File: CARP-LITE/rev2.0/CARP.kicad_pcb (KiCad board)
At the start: 4 copper layers, 70.1 x 40 mm, 154 parts, among them J1 USB-C, J10 PYRO_2, J11 RF_L, J3 I2C1+3V3, J4 2S XT30, J5 UART+5V+I2C1, J6 PYRO_1, J7 RF_H, J8 PWM1+5V1, J9 PWM2+5V1, Q5 SQ2318CES, Q6 SQ2318CES, Q7 SQ2318CES, SW1 SW_Push, SW2 SW_Push, U1 W25Q128JVSIMTR (16MB), U10 TPS62130A, U2 W25Q32RVXHJQ (2MB), U4 RP2350_60QFN, U5 LSM6DSO, U6 BMP390, U7 TLV75733PDBV, U9 LR2021IMLTRT, Y1 ABM8-272-T3, Y2 ECS-TXO-25CSMV-320-AN-TR

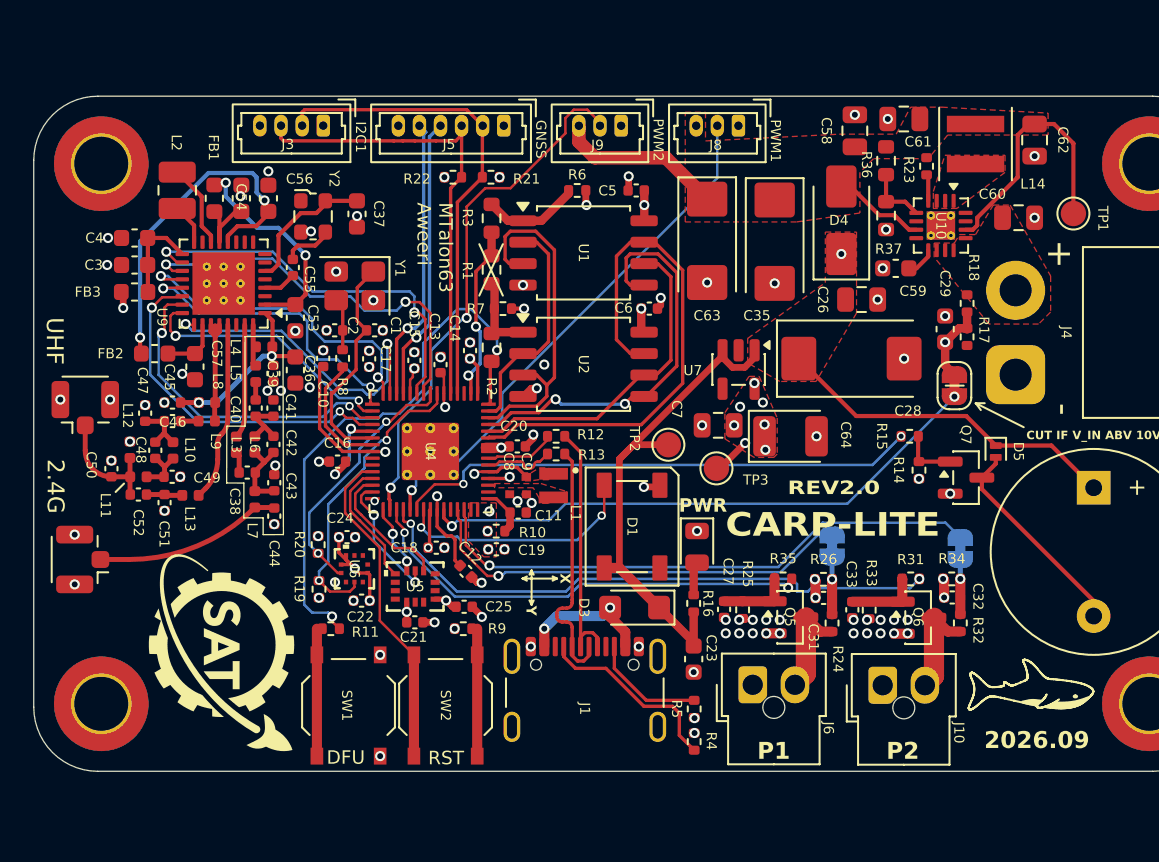
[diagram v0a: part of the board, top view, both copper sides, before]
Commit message: move vias from pads
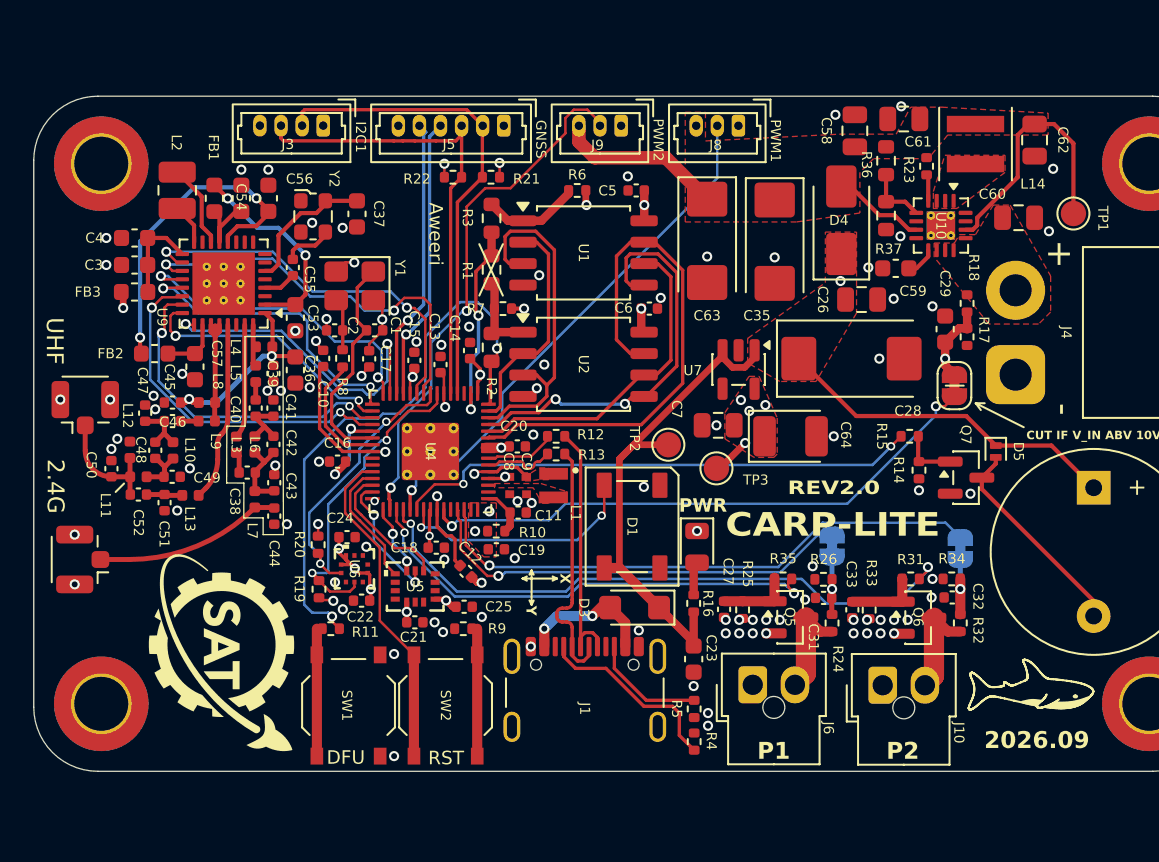
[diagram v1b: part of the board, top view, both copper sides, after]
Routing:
- net +3V3: track 32.5 -> 36.4 mm, vias 33 -> 29
- net GND: track 10.4 -> 7.97 mm, vias 98 -> 94
- net /GPIO22: track 34.9 -> 37.1 mm
- net /GPIO0: track 10.4 -> 12.1 mm
- net +5V: track 86.4 -> 88.0 mm
- net Net-(U9-VDCC1): track 21.0 -> 19.6 mm
- net /QSPI_SS: track 33.3 -> 34.3 mm
- net /GPIO5: track 15.3 -> 16.3 mm
- net /GPIO21: track 27.4 -> 28.4 mm
- net /Radio/VR_PA: track 11.3 -> 12.1 mm
- net /GPIO4: track 17.7 -> 18.5 mm
- net /GPIO29_ADC3: track 3.25 -> 3.85 mm
- net /GPIO28_ADC2: track 3.40 -> 4.00 mm
- net Net-(U9-VPAX2): track 12.7 -> 12.1 mm
- net /GPIO6: track 23.6 -> 24.2 mm
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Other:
- board text added: "Aweeri"
- board text removed: "MTalon63 Aweeri"

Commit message: IMU interrupt GPIO fix
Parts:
- removed C38: 18p, Capacitor_SMD:C_0402_1005Metric
- removed C39: 470p, Capacitor_SMD:C_0402_1005Metric
- removed C40: 6.8p, Capacitor_SMD:C_0402_1005Metric
- removed C41: 2.7p, Capacitor_SMD:C_0402_1005Metric
- removed C42: 1.1p, Capacitor_SMD:C_0402_1005Metric
- removed C43: 1.2p, Capacitor_SMD:C_0402_1005Metric
- removed C44: 2.0p, Capacitor_SMD:C_0402_1005Metric
- removed C5: 100n, Capacitor_SMD:C_0402_1005Metric
- removed J7: RF_H, Connector_Coaxial:U.FL_Hirose_U.FL-R-SMT-1_Vertical
- removed L3: 2.4n, Inductor_SMD:L_0402_1005Metric
- removed L4: 18n, Inductor_SMD:L_0402_1005Metric
- removed L5: 1.7n, Inductor_SMD:L_0402_1005Metric
- removed L6: 1.9n, Inductor_SMD:L_0402_1005Metric
- removed L7: 1n, Inductor_SMD:L_0402_1005Metric
- removed R1: DNF, Resistor_SMD:R_0603_1608Metric
- removed R3: 0, Resistor_SMD:R_0603_1608Metric
- removed R6: 5.1k, Resistor_SMD:R_0402_1005Metric
- removed U1: W25Q128JVSIMTR (16MB), Package_SO:SOIC-8_5.3x5.3mm_P1.27mm
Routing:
- net /QSPI_SD3: track 31.4 -> 14.9 mm
- net /QSPI_SD2: track 20.7 -> 6.44 mm
- net /QSPI_SD0: track 24.5 -> 10.3 mm
- net /GPIO0: track 12.1 -> 0.00 mm, vias 2 -> 0
- net Net-(J7-In): track 11.2 -> 0.00 mm
- net /QSPI_SCLK: track 19.4 -> 11.3 mm
- net /QSPI_SD1: track 13.4 -> 5.44 mm
- net /Radio/RFI_HF: track 6.74 -> 0.00 mm
- net /FLASH2_SS: track 5.82 -> 0.00 mm
- net Net-(C38-Pad2): track 4.71 -> 0.00 mm
- net Net-(C40-Pad1): track 3.49 -> 0.00 mm
- net +3V3: track 36.4 -> 33.7 mm, vias 29 -> 27
- net /Radio/RFO_HF: track 2.48 -> 0.00 mm
- net /FLASH1_SS: track 5.10 -> 3.55 mm
- net Net-(C38-Pad1): track 1.24 -> 0.00 mm
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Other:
- board text removed: "2.4G"

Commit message: mess up pcb a bit
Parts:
- removed D4: VSSAF5L45, Diode_SMD:D_SMA
- removed U6: BMP390, bmp_fps:10LGA_2X2X0p75_BOS
- added C30: 100n, Capacitor_SMD:C_0402_1005Metric, F.Cu at (508.6, 281.7)
- added C34: 100n, Capacitor_SMD:C_0402_1005Metric, F.Cu at (508.6, 283.6)
- added C5: 100n, Capacitor_SMD:C_0402_1005Metric, F.Cu at (508.6, 279.7)
- added C65: 4.7u, Capacitor_SMD:C_0603_1608Metric, F.Cu at (521.8, 280.1)
- added C66: 47n, Capacitor_SMD:C_0402_1005Metric, F.Cu at (508.6, 285.6)
- added C67: 47n, Capacitor_SMD:C_0402_1005Metric, F.Cu at (508.6, 287.6)
- added C68: 47n, Capacitor_SMD:C_0402_1005Metric, F.Cu at (508.6, 289.5)
- added C69: 1n, Capacitor_SMD:C_0603_1608Metric, F.Cu at (525.7, 282.1)
- added C70: 10u, Capacitor_SMD:C_0805_2012Metric, F.Cu at (491.4, 271.2)
- added C71: 10u, Capacitor_SMD:C_0805_2012Metric, F.Cu at (491.4, 274.2)
- added C72: 10u, Capacitor_SMD:C_0805_2012Metric, F.Cu at (491.4, 277.2)
- added C73: 10u, Capacitor_SMD:C_0805_2012Metric, F.Cu at (491.4, 280.2)
- added C74: 10u, Capacitor_SMD:C_0805_2012Metric, F.Cu at (491.4, 283.2)
- added C75: 10u, Capacitor_SMD:C_0805_2012Metric, F.Cu at (491.4, 286.2)
- added C76: 10u, Capacitor_SMD:C_0805_2012Metric, F.Cu at (491.4, 289.3)
- added J7: SPI, Connector_Molex:Molex_PicoBlade_53047-0610_1x06_P1.25mm_Vertical, F.Cu at (499.9, 310.9)
- added L15: 2.2u, Inductor_SMD:L_Coilcraft_XFL2010, F.Cu at (520.9, 288.1)
- added R28: 8.2k, Resistor_SMD:R_0402_1005Metric, F.Cu at (511.5, 279.7)
- added R38: 100, Resistor_SMD:R_0402_1005Metric, F.Cu at (511.5, 281.7)
- added R39: 5.1k, Resistor_SMD:R_0402_1005Metric, F.Cu at (511.5, 283.7)
- added R40: 5.1k, Resistor_SMD:R_0402_1005Metric, F.Cu at (511.5, 285.7)
- added R41: 1k, Resistor_SMD:R_0402_1005Metric, F.Cu at (511.5, 287.7)
- added REF**: Molex_Nano-Fit_105313-xx02_1x02_P2.50mm_Horizontal, Connector_Molex:Molex_Nano-Fit_105313-xx02_1x02_P2.50mm_Horizontal, B.Cu at (447.6, 301.7)
- added U1: BQ25792, Package_DFN_QFN:Texas_RQM0029A_VQFN-29_4x4mm_P0.4mm, F.Cu at (453.1, 315.6)
- added U3: BMP581, bmp_fps:10LGA_2X2X0p75_BOS, F.Cu at (412.5, 291.8)
- C3, C36, C37: footprint Capacitor_SMD:C_0603_1608Metric -> Capacitor_SMD:C_0402_1005Metric
- C31, C32: value 100n -> 1n
- D3: value V2FL45 -> CHARGER; footprint Diode_SMD:D_SMF -> LED_SMD:LED_0805_2012Metric
- J4: value 2S XT30 -> 2/3S XT30
- U2: value W25Q32RVXHJQ (2MB) -> W25Q128JVSIMTR (16MB)
- moved C24 85.7 mm to (497.9, 292.6), turned to 0 degrees
- moved C22 84.3 mm to (497.3, 295.4)
- moved D3 81.2 mm to (510.1, 300.4), turned to 0 degrees
- moved C4 1.60 mm to (399.6, 273.4)
- moved C3 1.38 mm to (399.9, 272.1)
- moved C37 0.40 mm to (412.4, 270.5)
- moved J4 0.05 mm to (451.8, 279.9)
- renumbered PWR to D2
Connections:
- C22 pad 1: GND -> +3V3
- C22 pad 2: +3V3 -> GND
- C24 pad 1: GND -> +3V3
- C24 pad 2: +3V3 -> GND
- C35 pad 1: +5V1 -> +5V
- C58 pad 1: +5V1 -> +5V
- C60 pad 2: +2S -> /CHRGR_OUT
- C61 pad 1: +5V1 -> +5V
- C62 pad 1: +5V1 -> +5V
- C63 pad 1: +5V1 -> +5V
- D1 pad 4: /GPIO25 -> /GPIO1
- D3 pad 1: +5V -> Net-(D3-K)
- D3 pad 2: /VBUS -> Net-(D3-A)
- J10 pad 1: +2S -> /BAT
- J4 pad 2: +2S -> /BAT
- J6 pad 1: +2S -> /BAT
- J8 pad 3: +5V1 -> +5V
- J9 pad 3: +5V1 -> +5V
- L14 pad 2: +5V1 -> +5V
- R23 pad 1: +5V1 -> +5V
- R36 pad 1: +5V1 -> +5V
- TP1 pad 1: +5V1 -> +5V
- U10 pad 10: +2S -> /CHRGR_OUT
- U10 pad 11: +2S -> /CHRGR_OUT
- U10 pad 12: +2S -> /CHRGR_OUT
- U10 pad 13: +2S -> /CHRGR_OUT
- U10 pad 14: +5V1 -> +5V
- U10 pad 7: +5V1 -> +5V
- U4 pad 3: unconnected-(U4-GPIO1-Pad3) -> /GPIO1
- U5 pad 4: unconnected-(U5-INT1-Pad4) -> /GPIO7
- U9 pad 18: /GPIO7 -> unconnected-(U9-DIO6-Pad18)
- U9 pad 31: /Radio/RFI_HF -> unconnected-(U9-RFI_HF-Pad31)
- U9 pad 32: /Radio/RFO_HF -> unconnected-(U9-RFO_HF-Pad32)
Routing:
- net +5V1: track 30.8 -> 0.00 mm
- net /GPIO25: track 14.6 -> 0.00 mm, vias 2 -> 0
- net +5V: track 88.0 -> 95.3 mm, vias 1 -> 0
- net +3V3: track 33.7 -> 26.9 mm, vias 27 -> 24
- net /GPIO4: track 18.5 -> 14.2 mm, vias 2 -> 1
- net /GPIO5: track 16.3 -> 12.8 mm, vias 2 -> 1
- net /VBUS: track 8.39 -> 7.37 mm
- net /GPIO3: track 28.3 -> 27.5 mm
- net /BAT: track 0.00 -> 0.60 mm
- net +2S: track 0.60 -> 0.00 mm
- net GND: vias 86 -> 83
- added copper zone on F.Cu, net /BAT
- added copper zone on In2.Cu, net /BAT
- removed copper zone on F.Cu, net +2S
- removed copper zone on In2.Cu, net +2S
- removed copper zone on F.Cu, net +5V1
